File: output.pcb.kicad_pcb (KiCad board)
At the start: 2 copper layers, 204.1 x 106.9 mm, 74 parts, among them J1 RPi_Header, J1 USB_B_Micro, J2 Conn_01x05, J2 Smoke_Sensor, J3 LEDs, J4 Temp_Sensor, J5 Alarm, J6 Conn_01x03, J7 Fan_Power, J8 USB_Power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

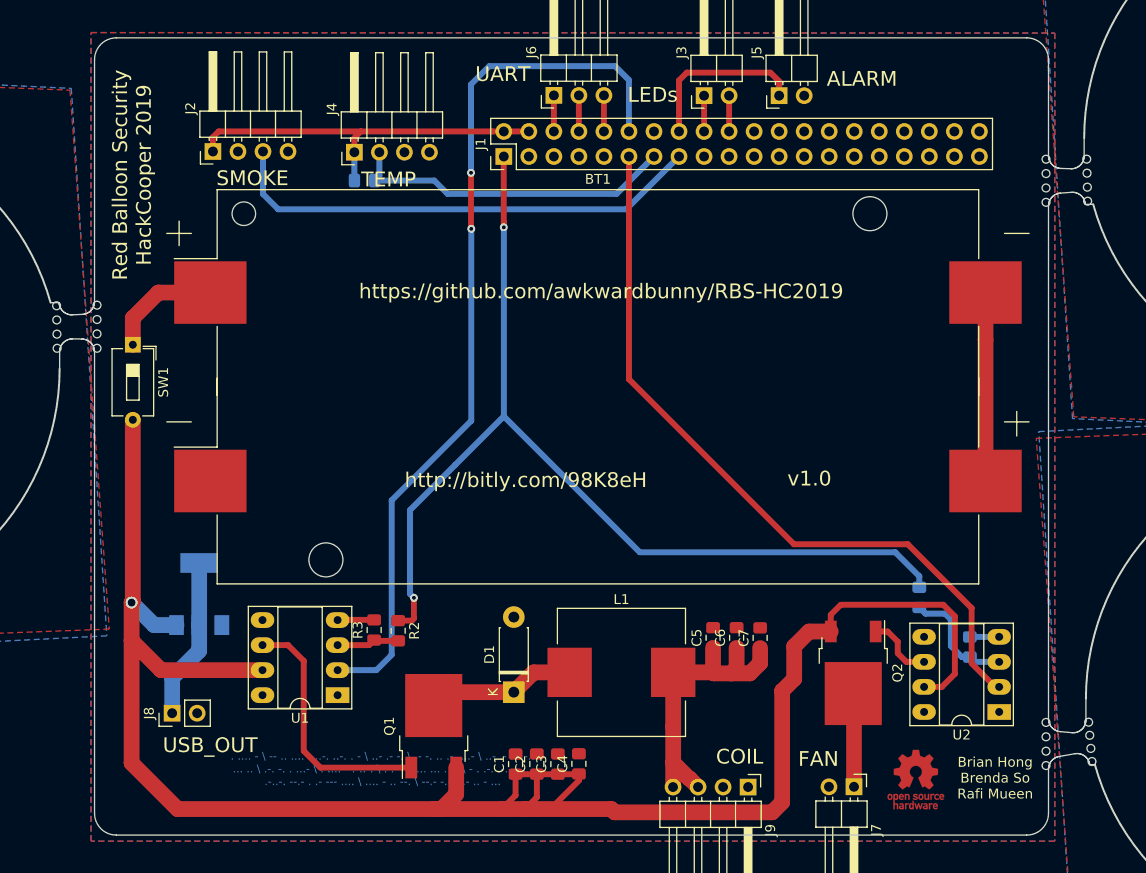
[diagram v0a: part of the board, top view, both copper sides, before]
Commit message: Thicker tabs for JLCPCB (>3mm)
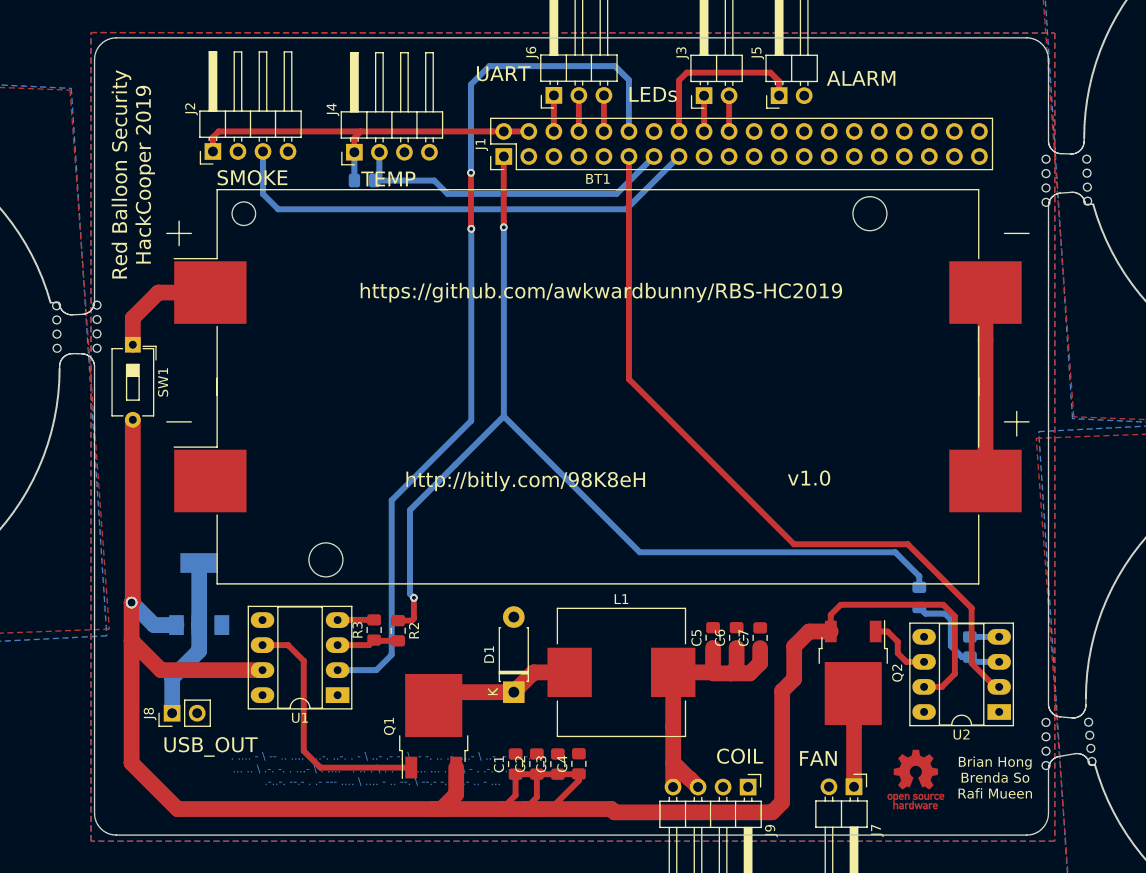
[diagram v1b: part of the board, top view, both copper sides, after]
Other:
- outline, holes or cut-outs redrawn
